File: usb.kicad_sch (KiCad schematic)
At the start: 140 parts, among them J3 USB-C_GCT_USB4105-GF-A, J4 USB-C_WE_632723300011, Q20 PJE138K, Q21 PJE138K, U10 TUSB1046-DCIRNQ, U11 TPD4E05U06QDQARQ1, U12 AP22615A_TSOT26, U13 TPD4E05U06QDQARQ1, U14 TPD4E05U06QDQARQ1, U15 TPD4E05U06QDQARQ1, U16 TPD4E05U06QDQARQ1, U47 NTS0102_XSON, U5 FT230X_QFN, U6 TPS65988DHRSHR, U7 W25Q80DV_USON, U8 NCP730BMT330_WSON, U9 AP22615A_TSOT26

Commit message: Init commit
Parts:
- C136, C148: LCSC Part # (none) -> C5846150
- C140, C141, C143, C144, C158, C159, C26, C27, C29, C31, C33, C36, C37, C45, C53, C54, C55, C57, C58, C60, C61, C62, C63, C64, C65: LCSC Part # (none) -> C85960
- C145, C146: LCSC Part # (none) -> C2169042
- C147, C149: LCSC Part # (none) -> C3898487
- C28, C30, C34, C35, C49, C56, C59: LCSC Part # (none) -> C105884
- C32: LCSC Part # (none) -> C2168289
- D2, D3, D4, D5, D8, D9: LCSC Part # (none) -> C125093
- D35: LCSC Part # (none) -> C145179
- D6, D7: LCSC Part # (none) -> C1973663
- J3: LCSC Part # (none) -> C3025063
- Q20, Q21: LCSC Part # (none) -> C391643
- R104, R78: LCSC Part # (none) -> C2076845
- R105, R106, R130, R246, R262, R81: LCSC Part # (none) -> C2076851
- R109, R110: LCSC Part # (none) -> C138014
- R111, R267, R85, R86, R87, R88, R89, R90, R91, R92, R93, R94, R95, R96, R97, R98: LCSC Part # (none) -> C202394
- R117, R127: LCSC Part # (none) -> C19946387
- R131, R42, R44, R46, R74, R77, R83, R99: LCSC Part # (none) -> C202396
- R144, R158, R244, R41, R56, R57, R58, R59, R65, R70, R71, R75, R76, R79, R82, R84: LCSC Part # (none) -> C242160
- R205, R207, R270, R43, R45: LCSC Part # (none) -> C2077080
- R271: LCSC Part # (none) -> C5628762
- R33: LCSC Part # (none) -> C1731295
- R68, R69, R72, R73: LCSC Part # (none) -> C19946422
- U10: LCSC Part # (none) -> C2652434
- U11, U13, U14, U15, U16: LCSC Part # (none) -> C81353
- U12, U9: LCSC Part # (none) -> C2680357
- U47: LCSC Part # (none) -> C2687851
- U6: LCSC Part # (none) -> C2156209
- U7: LCSC Part # (none) -> C401667
- U8: LCSC Part # (none) -> C892821

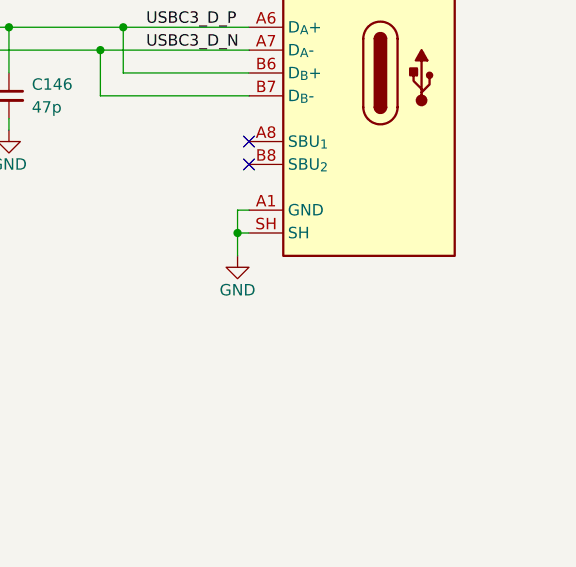
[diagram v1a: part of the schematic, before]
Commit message: Add field Digikey Part Number. Add Chinese substitute components
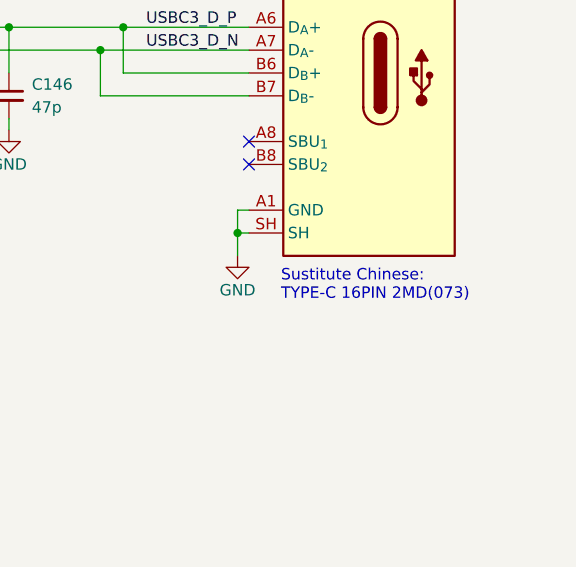
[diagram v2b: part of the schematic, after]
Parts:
- C136, C148: Digikey Part # (none) -> 490-GRM155C61E475ME15JCT-ND
- C140, C141, C143, C144, C158, C159, C26, C27, C29, C31, C33, C36, C37, C45, C53, C54, C55, C57, C58, C60, C61, C62, C63, C64, C65: Digikey Part # (none) -> 490-10697-1-ND
- C145, C146: Alternative MPN (none) -> 0402CG470J500NT; Digikey Part # (none) -> 399-C0402C470J5GACTUCT-ND
- C147, C149: Alternative MPN (none) -> CL05A105KA5NQNC; Digikey Part # (none) -> 490-GRM155R61E105KE11JCT-ND
- C28, C30, C34, C35, C49, C56, C59: Alternative MPN (none) -> CL05A106MQ5NUNC; Digikey Part # (none) -> 311-1729-1-ND
- C32: Alternative MPN (none) -> CL10A106MA8NRNC; Digikey Part # (none) -> 445-9015-1-ND
- D2, D3, D4, D5, D8, D9: Alternative MPN (none) -> LTST-C190KRKT; Digikey Part # (none) -> 160-1183-1-ND
- D35: Digikey Part # (none) -> RB521S30T1GOSCT-ND
- D6, D7: Digikey Part # (none) -> DF2S30FSL3MCT-ND
- J3: Digikey Part # (none) -> 2073-USB4105-GF-ACT-ND
- J4: Digikey Part # (none) -> 732-9618-1-ND
- Q20, Q21: Digikey Part # (none) -> 3757-PJE138K_R1_00001CT-ND
- R104, R78: Digikey Part # (none) -> CR0402-FX-2201GLFCT-ND
- R105, R106, R130, R246, R262, R81: Digikey Part # (none) -> CR0402-FX-4701GLFCT-ND
- R109, R110: Digikey Part # (none) -> 13-RC0402FR-072MLCT-ND
- R111, R267, R85, R86, R87, R88, R89, R90, R91, R92, R93, R94, R95, R96, R97, R98: Digikey Part # (none) -> CR0402-FX-1001GLFCT-ND
- R117, R127: Digikey Part # (none) -> CR0402-FX-27R0GLFCT-ND
- R131, R42, R44, R46, R74, R77, R83, R99: Digikey Part # (none) -> CR0402-FX-1002GLFCT-ND
- R144, R158, R244, R41, R56, R57, R58, R59, R65, R70, R71, R75, R76, R79, R82, R84: Digikey Part # (none) -> P0.0JCT-ND
- R205, R207, R270, R43, R45: Digikey Part # (none) -> CR0402-FX-1003GLFCT-ND
- R33: Digikey Part # (none) -> Y6000CT-ND
- R68, R69, R72, R73: Digikey Part # (none) -> CR0402-FX-2000GLFCT-ND
- U10: Digikey Part # (none) -> 296-44772-1-ND
- U11, U13, U14, U15, U16: Digikey Part # (none) -> 296-40696-1-ND
- U12, U9: Digikey Part # (none) -> AP22615AWU-7DICT-ND
- U47: Digikey Part # (none) -> 568-5205-1-ND
- U5: Digikey Part # (none) -> 768-1130-1-ND
- U6: Digikey Part # (none) -> 296-52068-1-ND
- U7: Digikey Part # (none) -> W25Q80DVUXIECT-ND
- U8: Digikey Part # (none) -> 488-NCP730BMT330TBGCT-ND
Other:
- note added: "Sustitute Chinese: TYPE-C 16PIN 2MD(073)"
